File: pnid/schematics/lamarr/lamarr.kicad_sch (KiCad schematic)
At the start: 72 parts

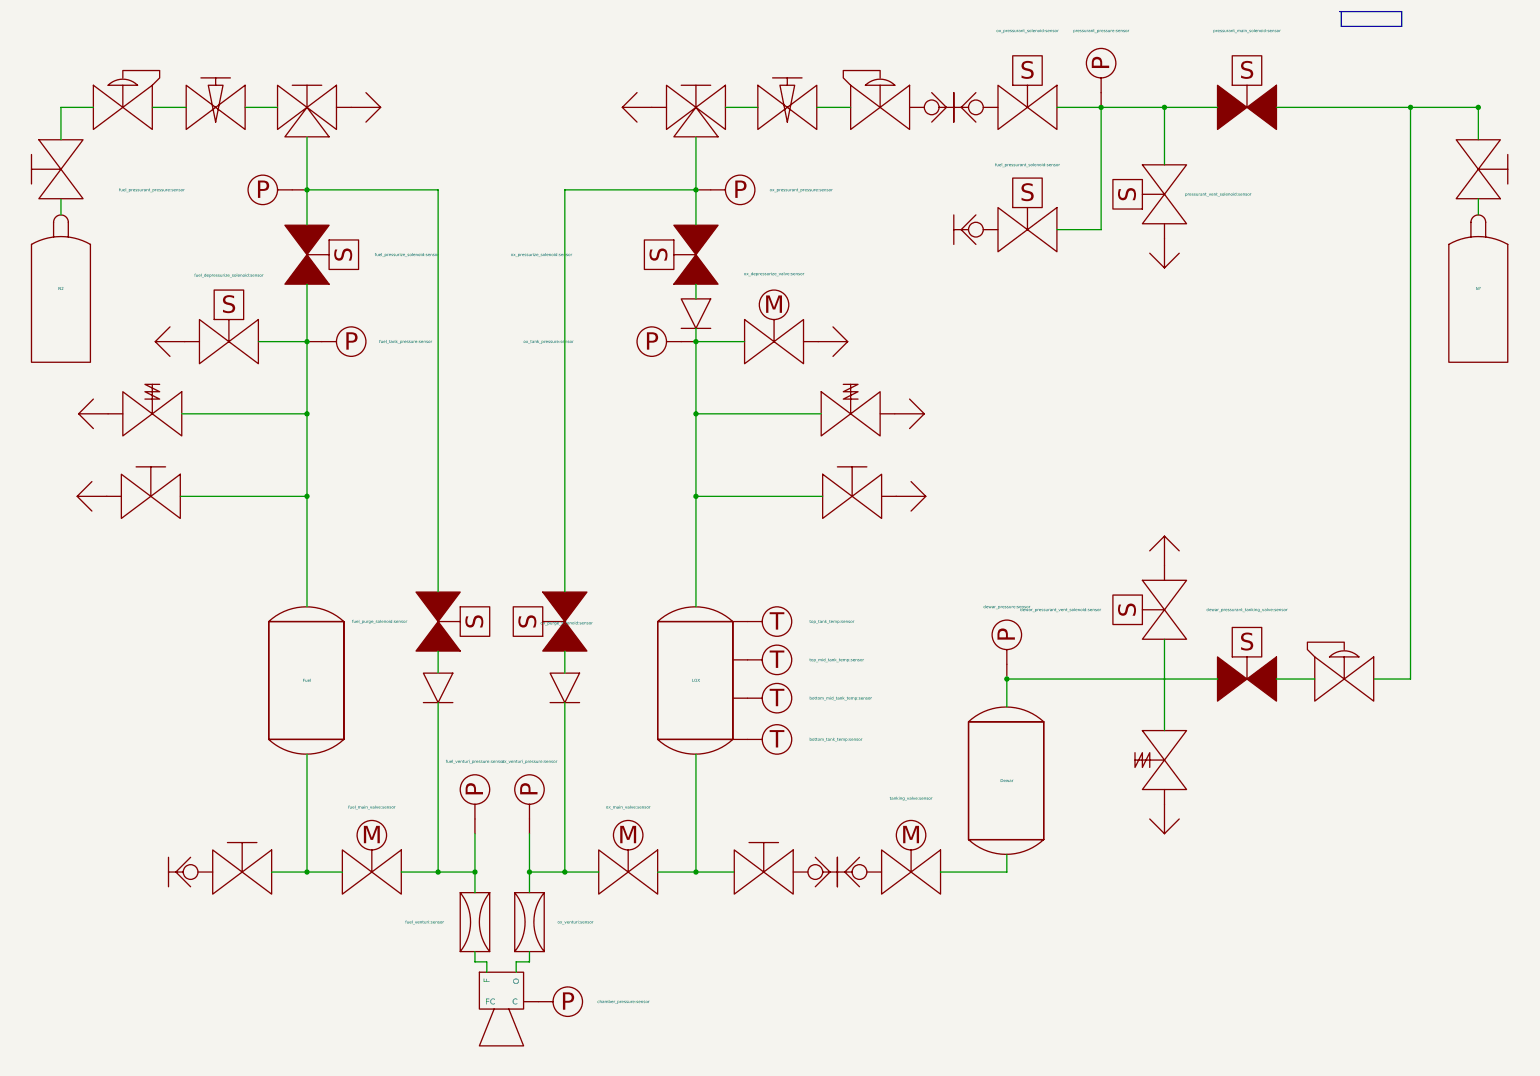
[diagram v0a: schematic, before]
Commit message: update label placement for lamarr pnid
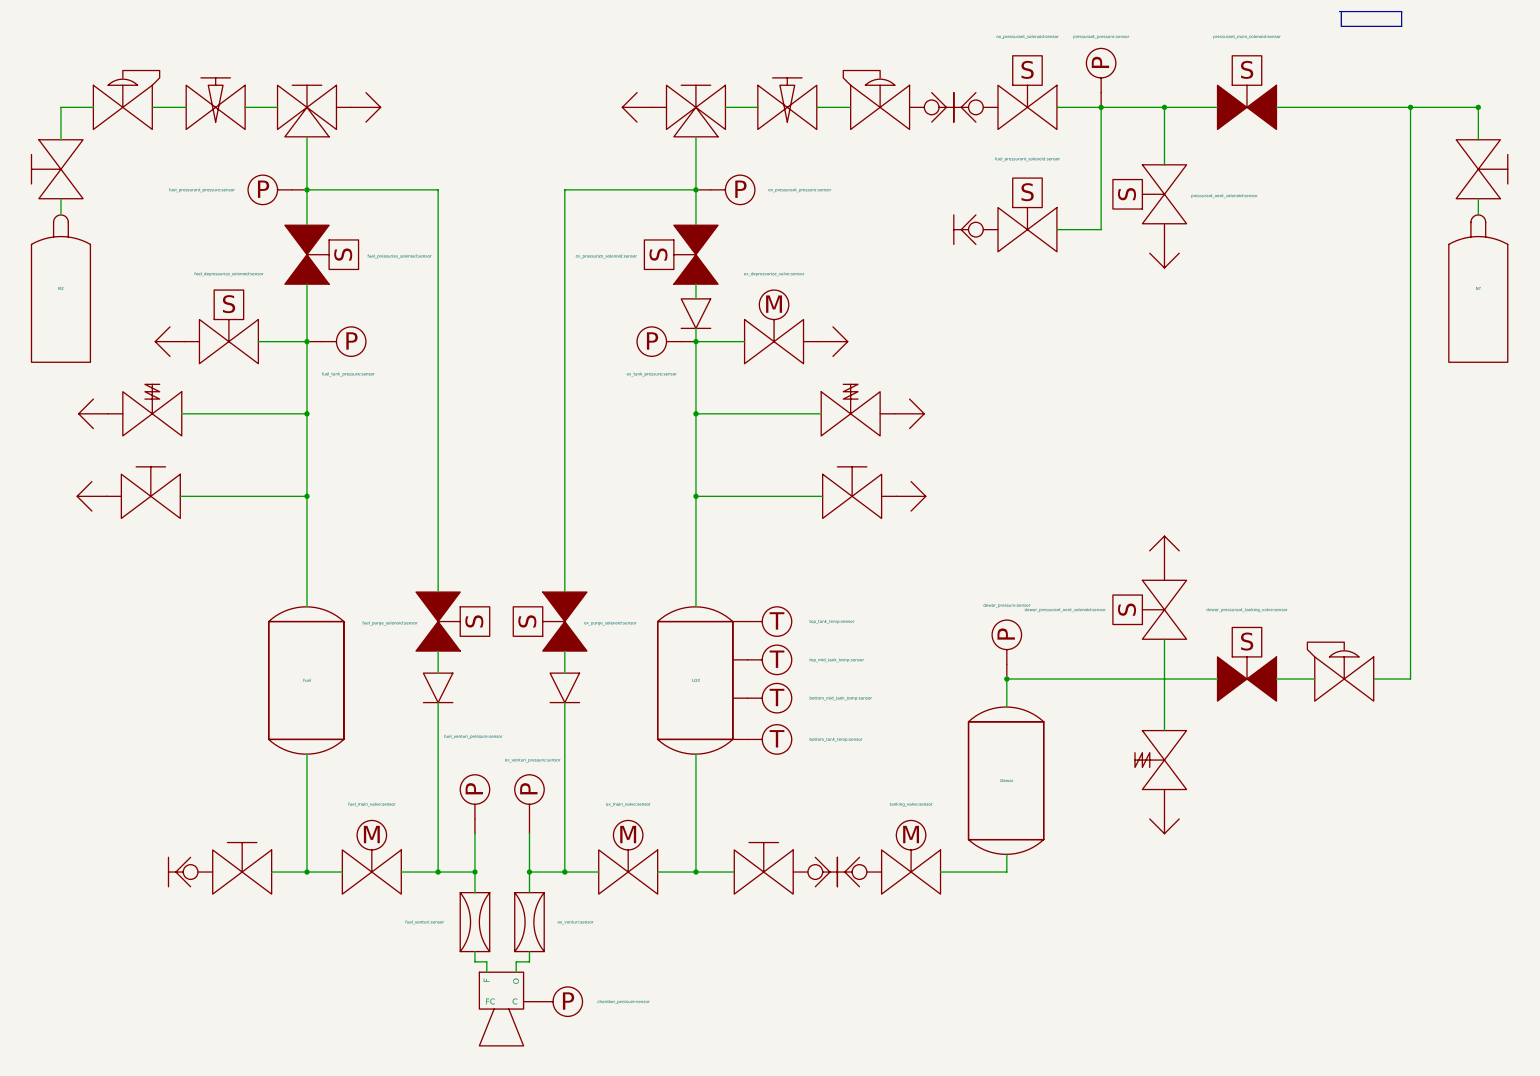
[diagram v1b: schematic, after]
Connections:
- net at engine.~ (O): now also fuel_venturi.~
- net at ox_venturi.~: now also CheckValve?.~, ox_main_valve.~, ox_venturi_pressure.~; no longer engine.~ (O)
- net at fuel_venturi.~: now also CheckValve?.~, fuel_main_valve.~, fuel_venturi_pressure.~; no longer engine.~ (O)
- net at DewarPressureRegulator?.~: now also ox_manual_valve.~, pressurant_main_solenoid?.~; no longer dewar_pressurant_tanking_valve?.~
- net at DewarOverPressureValve?.~: now also Vent?.~; no longer dewar_pressurant_vent_solenoid?.~
- new net: fuel_manual_3way?.~, ox_pressurant_pressure:sensor.~, ox_pressurize_solenoid.~, ox_purge_solenoid.~
- new net: fuel_manual_3way.~, fuel_pressurant_pressure.~, fuel_pressurize_solenoid.~, fuel_purge_solenoid.~
- new net: Fuel.~, fuel_depressurize_solenoid.~, fuel_manual_vent_valve.~, fuel_pressurize_solenoid.~, fuel_safety_valve.~, fuel_tank_pressure.~
- new net: CheckValve?.~, LOX.~, ox_depressurize_valve.~, ox_manual_vent_valve.~, ox_safety_valve.~, ox_tank_pressure.~
- new net: LOX.~, ox_main_valve.~, ox_manual_tanking_valve.~
- new net: Fuel.~, fuel_main_valve.~, fuel_manual_tanking_valve.~
- new net: engine.~ (O), ox_venturi.~
- new net: DewarPressureRegulator?.~, dewar_pressurant_tanking_valve?.~
- new net: DewarOverPressureValve?.~, dewar_pressurant_vent_solenoid?.~
- new net: fuel_pressurant_solenoid?.~, ox_pressurant_solenoid?.~, pressurant_main_solenoid?.~, pressurant_pressure?.~, pressurant_vent_solenoid?.~
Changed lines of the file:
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@@
 		)
 		(property "Value" "ox_pressurant_pressure:sensor"
-			(at 148.082 45.212 0)
+			(at 147.828 45.212 0)
 			(effects
 				(font
@@
 		)
 		(property "Value" "fuel_pressurant_pressure:sensor"
-			(at 47.244 45.212 0)
+			(at 55.88 45.212 0)
 			(effects
 				(font
@@
 	)
 	(symbol
+		(lib_name "PnID-Lib:Valve_Solenoid_NC")
 		(lib_id "PnID-Lib:Valve_Solenoid_NC")
 		(at 135.382 56.388 90)
@@
 		)
 		(property "Value" "ox_pressurize_solenoid:sensor"
-			(at 114.046 56.388 90)
+			(at 125.222 56.642 90)
 			(effects
 				(font
@@
 	)
 	(symbol
+		(lib_name "PnID-Lib:Valve_Solenoid_NC")
 		(lib_id "PnID-Lib:Valve_Solenoid_NC")
 		(at 68.326 56.388 270)
@@
 		)
 		(property "Value" "fuel_pressurize_solenoid:sensor"
-			(at 80.01 56.388 90)
+			(at 78.74 56.642 90)
 			(effects
 				(font
@@
 	)
 	(symbol
+		(lib_name "PnID-Lib:Valve_Solenoid_NC")
 		(lib_id "PnID-Lib:Valve_Solenoid_NC")
 		(at 112.776 119.634 90)
@@
 		)
 		(property "Value" "ox_purge_solenoid:sensor"
-			(at 117.602 119.888 90)
+			(at 116.078 119.888 90)
 			(effects
 				(font
 					(size 0.508 0.508)
 				)
-				(justify left)
+				(justify right)
 			)
 		)
@@
 	)
 	(symbol
+		(lib_name "PnID-Lib:Valve_Solenoid_NC")
 		(lib_id "PnID-Lib:Valve_Solenoid_NC")
 		(at 90.932 119.634 270)
@@
 		)
 		(property "Value" "fuel_purge_solenoid:sensor"
-			(at 85.598 119.634 90)
+			(at 87.376 119.888 90)
 			(effects
 				(font
@@
 		)
 		(property "Value" "fuel_venturi_pressure:sensor"
-			(at 97.282 143.764 90)
+			(at 91.948 139.446 90)
 			(effects
 				(font
 					(size 0.508 0.508)
 				)
+				(justify right)
 			)
 		)
@@
 		)
 		(property "Value" "ox_venturi_pressure:sensor"
-			(at 106.68 143.764 90)
+			(at 112.014 143.51 90)
 			(effects
 				(font
 					(size 0.508 0.508)
 				)
+				(justify left)
 			)
 		)
@@
 	)
 	(symbol
+		(lib_name "PnID-Lib:Valve_Solenoid_NO")
 		(lib_id "PnID-Lib:Valve_Solenoid_NO")
 		(at 54.864 71.374 0)
@@
 		)
 		(property "Value" "fuel_depressurize_solenoid:sensor"
-			(at 54.864 59.944 0)
+			(at 54.864 59.69 0)
 			(effects
 				(font
@@
 	)
 	(symbol
+		(lib_name "PnID-Lib:Valve_Servo")
 		(lib_id "PnID-Lib:Valve_Servo")
 		(at 79.502 162.814 0)
@@
 		)
 		(property "Value" "fuel_main_valve:sensor"
-			(at 79.502 151.638 0)
+			(at 79.502 151.13 0)
 			(effects
 				(font
@@
 		)
 		(property "Value" "dewar_pressure:sensor"
-			(at 188.976 117.094 90)
+			(at 188.976 116.84 90)
 			(effects
 				(font
@@
 	)
 	(symbol
+		(lib_name "PnID-Lib:Valve_Servo")
 		(lib_id "PnID-Lib:Valve_Servo")
 		(at 172.466 162.814 0)
@@
 		)
 		(property "Value" "tanking_valve:sensor"
-			(at 172.466 150.114 0)
+			(at 172.466 151.13 0)
 			(effects
 				(font
@@
 	)
 	(symbol
+		(lib_name "PnID-Lib:Valve_Solenoid_NC")
 		(lib_id "PnID-Lib:Valve_Solenoid_NC")
 		(at 230.378 30.988 0)
@@
 		)
 		(property "Value" "pressurant_main_solenoid:sensor"
-			(at 230.378 17.78 0)
+			(at 230.378 18.796 0)
 			(effects
 				(font
@@
 	)
 	(symbol
+		(lib_name "PnID-Lib:Valve_Solenoid_NO")
 		(lib_id "PnID-Lib:Valve_Solenoid_NO")
 		(at 216.154 45.974 90)
@@
 		)
 		(property "Value" "pressurant_vent_solenoid:sensor"
-			(at 231.14 45.974 90)
+			(at 220.726 46.228 90)
 			(effects
 				(font
 					(size 0.508 0.508)
 				)
-				(justify left)
+				(justify right)
 			)
 		)
@@
 		)
 		(property "Value" "pressurant_pressure:sensor"
-			(at 205.232 17.78 90)
+			(at 205.232 18.796 90)
 			(effects
 				(font
@@
 	)
 	(symbol
+		(lib_name "PnID-Lib:Valve_Solenoid_NO")
 		(lib_id "PnID-Lib:Valve_Solenoid_NO")
 		(at 192.532 52.07 0)
@@
 		)
 		(property "Value" "fuel_pressurant_solenoid:sensor"
-			(at 192.532 40.894 0)
+			(at 192.532 39.878 0)
 			(effects
 				(font
@@
 	)
 	(symbol
+		(lib_name "PnID-Lib:Valve_Solenoid_NO")
 		(lib_id "PnID-Lib:Valve_Solenoid_NO")
 		(at 192.532 30.988 0)
@@
 		)
 		(property "Value" "ox_pressurant_solenoid:sensor"
-			(at 192.532 17.78 0)
+			(at 192.532 18.796 0)
 			(effects
 				(font
@@
 	)
 	(symbol
+		(lib_name "PnID-Lib:Valve_Solenoid_NO")
 		(lib_id "PnID-Lib:Valve_Solenoid_NO")
 		(at 216.154 117.602 90)
@@
 		)
 		(property "Value" "dewar_pressurant_vent_solenoid:sensor"
-			(at 205.232 117.602 90)
+			(at 205.994 117.602 90)
 			(effects
 				(font
@@
 		)
 		(property "Value" "fuel_tank_pressure:sensor"
-			(at 80.772 71.374 0)
+			(at 70.866 76.962 0)
 			(effects
 				(font
@@
 		)
 		(property "Value" "ox_tank_pressure:sensor"
-			(at 114.3 71.374 0)
+			(at 132.08 76.962 0)
 			(effects
 				(font
@@
 	)
 	(symbol
+		(lib_name "PnID-Lib:Valve_Servo")
 		(lib_id "PnID-Lib:Valve_Servo")
 		(at 123.698 162.814 0)
@@
 		)
 		(property "Value" "ox_main_valve:sensor"
-			(at 123.698 151.638 0)
+			(at 123.698 151.13 0)
 			(effects
 				(font

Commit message: update lamarr pnid to be correct version
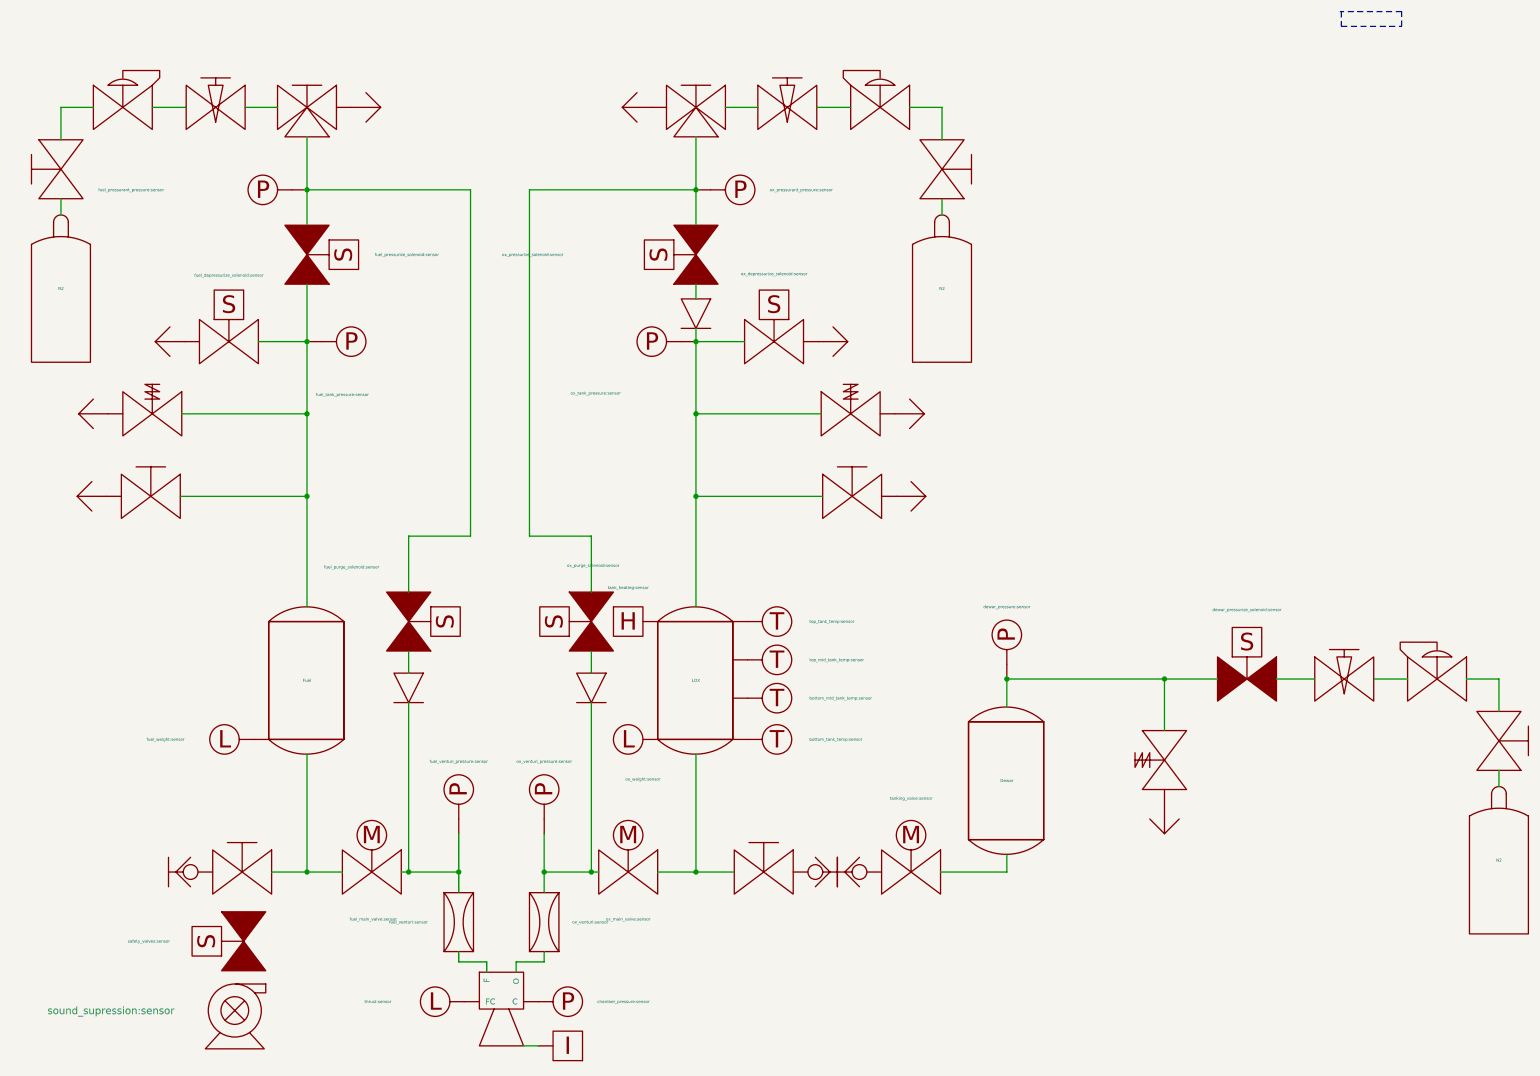
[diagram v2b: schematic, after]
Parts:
- removed DewarPressureRegulator?: DewarPressureRegulator, symbol PnID-Lib:PressureRegulator
- removed N?: N2, symbol PnID-Lib:GasBottle
- removed QuickConnect?: QuickConnect_Half, symbol PnID-Lib:QuickConnect_Half
- removed Vent? (x3): Vent, symbol PnID-Lib:Vent
- removed dewar_pressurant_vent_solenoid?: dewar_pressurant_vent_solenoid:sensor, symbol PnID-Lib:Valve_Solenoid_NO
- removed fuel_pressurant_solenoid?: fuel_pressurant_solenoid:sensor, symbol PnID-Lib:Valve_Solenoid_NO
- removed fuel_quick_connect?: fuel_quick_connect, symbol PnID-Lib:QuickConnect_Half
- removed ox_manual_valve: ox_manual_valve, symbol PnID-Lib:Valve_Manual
- removed ox_pressurant_solenoid?: ox_pressurant_solenoid:sensor, symbol PnID-Lib:Valve_Solenoid_NO
- removed ox_quick_connect?: ox_quick_connect, symbol PnID-Lib:QuickConnect_Half
- removed pressurant_main_solenoid?: pressurant_main_solenoid:sensor, symbol PnID-Lib:Valve_Solenoid_NC
- removed pressurant_pressure?: pressurant_pressure:sensor, symbol PnID-Lib:Sensor_Pressure
- removed pressurant_vent_solenoid?: pressurant_vent_solenoid:sensor, symbol PnID-Lib:Valve_Solenoid_NO
- added N2 (x2): N2, symbol PnID-Lib:GasBottle
- added U1: sound_supression:sensor, symbol PnID-Lib:Pump
- added Vent?: Vent, symbol PnID-Lib:Vent
- added dewar_manual_valve?: dewar_manual_valve, symbol PnID-Lib:Valve_Manual
- added dewar_needle_valve?: dewar_needle_valve, symbol PnID-Lib:Valve_Needle
- added dewar_pressure_regulator?: dewar_pressure_regulator, symbol PnID-Lib:PressureRegulator
- added fuel_weight: fuel_weight:sensor, symbol PnID-Lib:Sensor_Load
- added heater1: tank_heating:sensor, symbol PnID-Lib:heater
- added igniter: igniter:sensor, symbol PnID-Lib:igniter
- added ox_manual_valve?: ox_manual_valve, symbol PnID-Lib:Valve_Manual
- added ox_purge_solenoid1: safety_valves:sensor, symbol PnID-Lib:Valve_Solenoid_NC
- added ox_weight: ox_weight:sensor, symbol PnID-Lib:Sensor_Load_Short
- added thrust: thrust:sensor, symbol PnID-Lib:Sensor_Load
- dewar_pressurize_solenoid?: renamed from dewar_pressurant_tanking_valve?; value dewar_pressurant_tanking_valve:sensor -> dewar_pressurize_solenoid:sensor
- ox_depressurize_solenoid: renamed from ox_depressurize_valve; value ox_depressurize_valve:sensor -> ox_depressurize_solenoid:sensor; symbol PnID-Lib:Valve_Servo -> PnID-Lib:Valve_Solenoid_NO
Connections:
- net at engine.~ (O): now also thrust.~
- net at ox_venturi.~: now also CheckValve?.~, ox_main_valve.~, ox_venturi_pressure.~; no longer engine.~ (O)
- net at fuel_venturi.~: now also CheckValve?.~, fuel_main_valve.~, fuel_venturi_pressure.~; no longer engine.~ (O)
- net at dewar_pressurize_solenoid?.~: now also dewar_needle_valve?.~
- net at DewarOverPressureValve?.~: now also Vent?.~
- net at ox_pressure_regulator.~: now also ox_manual_valve?.~
- net at ox_manual_vent_valve.~: now also Vent?.~
- net at ox_needle_valve.~: now also fuel_manual_3way?.~; no longer ox_pressure_regulator.~
- new net: fuel_manual_3way?.~, ox_pressurant_pressure:sensor.~, ox_pressurize_solenoid.~, ox_purge_solenoid.~
- new net: fuel_manual_3way.~, fuel_pressurant_pressure.~, fuel_pressurize_solenoid.~, fuel_purge_solenoid.~
- new net: Fuel.~, fuel_depressurize_solenoid.~, fuel_manual_vent_valve.~, fuel_pressurize_solenoid.~, fuel_safety_valve.~, fuel_tank_pressure.~
- new net: CheckValve?.~, LOX.~, ox_depressurize_solenoid.~, ox_manual_vent_valve.~, ox_safety_valve.~, ox_tank_pressure.~
- new net: LOX.~, ox_main_valve.~, ox_manual_tanking_valve.~
- new net: Fuel.~, fuel_main_valve.~, fuel_manual_tanking_valve.~
- new net: engine.~ (O), ox_venturi.~
- new net: engine.~ (O), fuel_venturi.~
- new net: Dewar.~, DewarOverPressureValve?.~, dewar_pressure?.~, dewar_pressurize_solenoid?.~
- new net: ox_needle_valve.~, ox_pressure_regulator.~
- new net: N2.~, ox_manual_valve?.~
- new net: dewar_needle_valve?.~, dewar_pressure_regulator?.~
- new net: dewar_manual_valve?.~, dewar_pressure_regulator?.~
- new net: N2.~, dewar_manual_valve?.~
